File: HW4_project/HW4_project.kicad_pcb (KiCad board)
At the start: 2 copper layers, 50 x 50 mm, 26 parts, among them J1 CP2102, J2 BATT, J3 L, J4 R, J5 SCO, SW1 MCLR, SW2 SW_SPDT, SW3 USER, U1 AP7381-33V, U2 PIC32

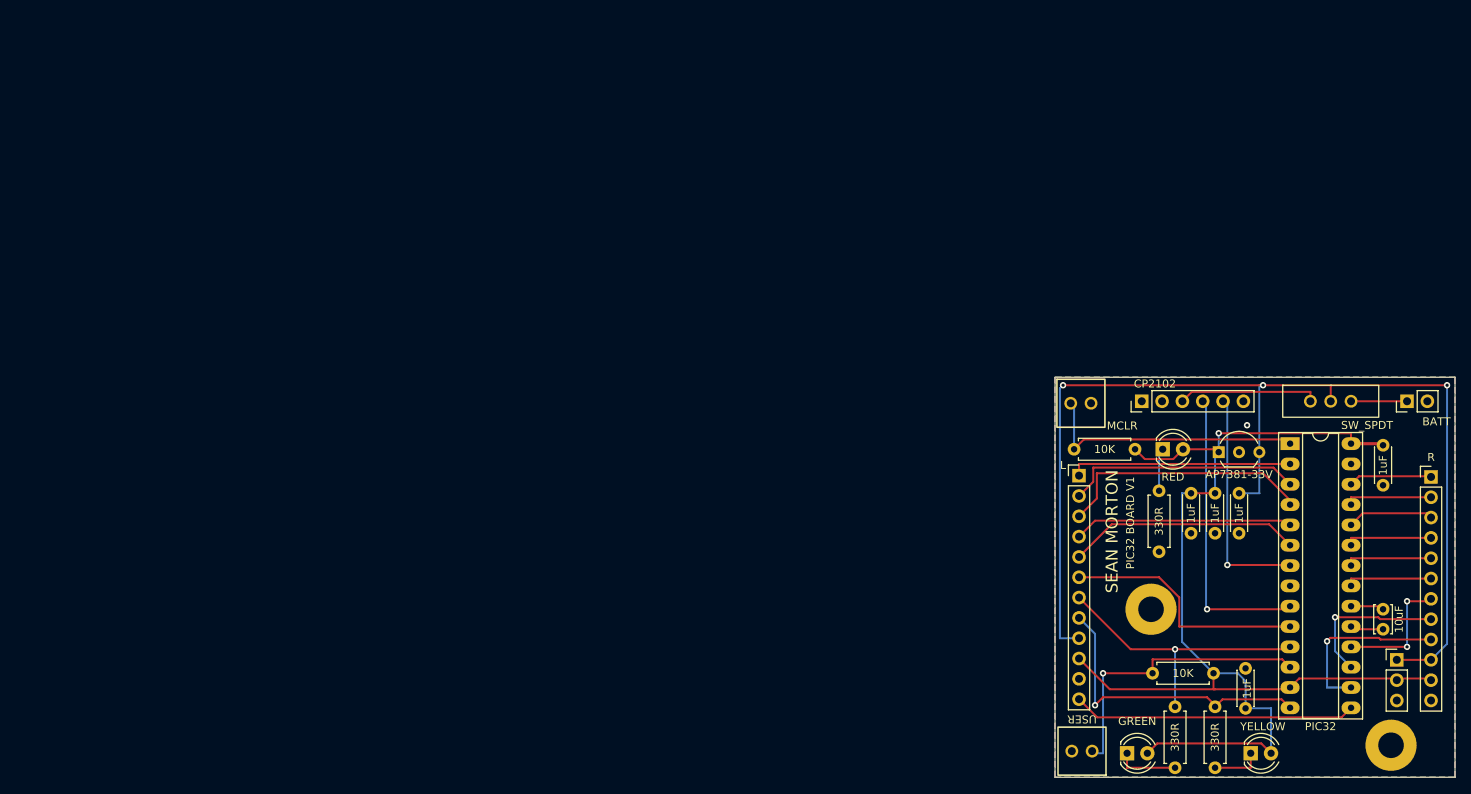
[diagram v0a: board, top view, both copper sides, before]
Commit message: HW4: silkscreen revisions
- added labels for all the broken-out pins
- fixed spacing on the button components
- added NURC logo
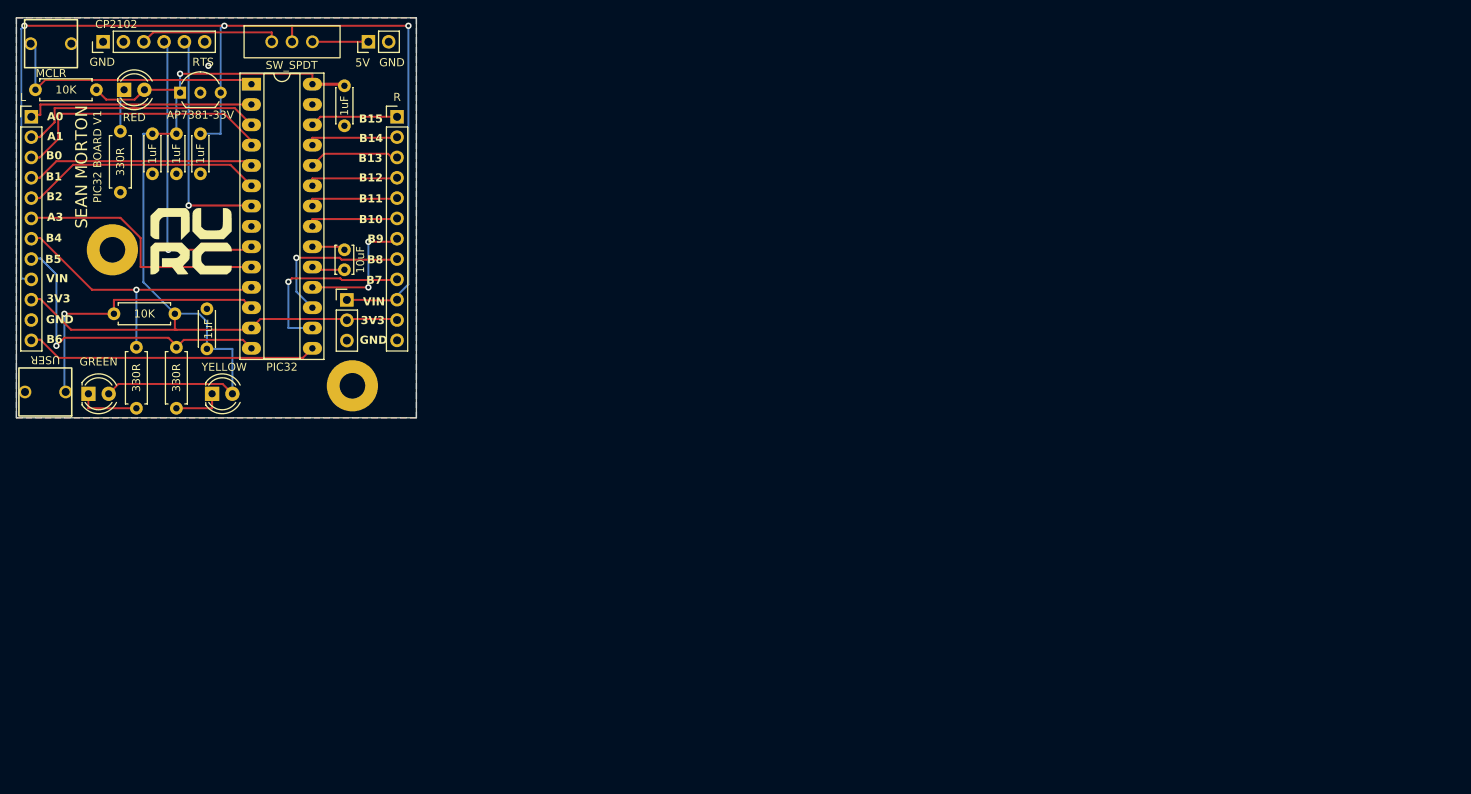
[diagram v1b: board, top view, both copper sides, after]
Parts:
- added G***: LOGO, HW4_footprints:logo_footprint_v3, F.Cu at (22.0, 28.0)
- moved J5 138.7 mm to (41.5, 35.3)
- moved J3 138.4 mm to (2.03, 12.4)
- moved C1 137.4 mm to (41.2, 8.57)
- moved C2 137.4 mm to (41.2, 29.1)
- moved D1 137.4 mm to (24.6, 47.1)
- moved D3 137.4 mm to (13.6, 9.07)
- moved H2 137.4 mm to (42.2, 46.1)
- moved J1 137.4 mm to (11.0, 3.07)
- moved J2 137.4 mm to (44.2, 3.07)
- moved SW2 137.4 mm to (34.6, 3.07)
- moved U1 137.4 mm to (20.6, 9.43)
- moved C3 137.4 mm to (20.2, 14.6)
- moved C4 137.4 mm to (17.2, 19.6)
- moved C5 137.4 mm to (24.0, 41.5)
- moved C7 137.4 mm to (23.2, 14.6)
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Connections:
- H2 pad 1: (no net) -> GND
- H3 pad 1: (no net) -> GND
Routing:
- net /RA1: track 29.8 -> 31.9 mm
- net /RA4_USER: track 37.3 -> 35.6 mm
- net /VDD5V0: track 139.2 -> 140.4 mm
- net /RB5_YLED: track 38.0 -> 39.1 mm
- net /RB4_GLED: track 36.5 -> 37.7 mm
- net /RB2: track 29.2 -> 30.3 mm
- net /RB0: track 32.4 -> 33.6 mm
- net /RA3: track 31.1 -> 32.2 mm
- net /RB1: track 27.4 -> 28.6 mm
- net /RB6: track 35.4 -> 36.6 mm
- net /VDD3V3: track 151.1 -> 152.3 mm
- net /RA0: track 27.8 -> 28.9 mm
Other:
- board text added: "3V3"
- board text added: "5V"
- board text added: "A0"
- board text added: "A1"
- board text added: "A3"
- board text added: "B0"
- board text added: "B1"
- board text added: "B10"
- board text added: "B11"
- board text added: "B12"
- board text added: "B13"
- board text added: "B14"
- board text added: "B15"
- board text added: "B2"
- board text added: "B4"
- board text added: "B5"
- board text added: "B6"
- board text added: "B7"
- board text added: "B8"
- board text added: "B9"
- board text added: "GND"
- board text added: "RTS"
- board text added: "VIN"

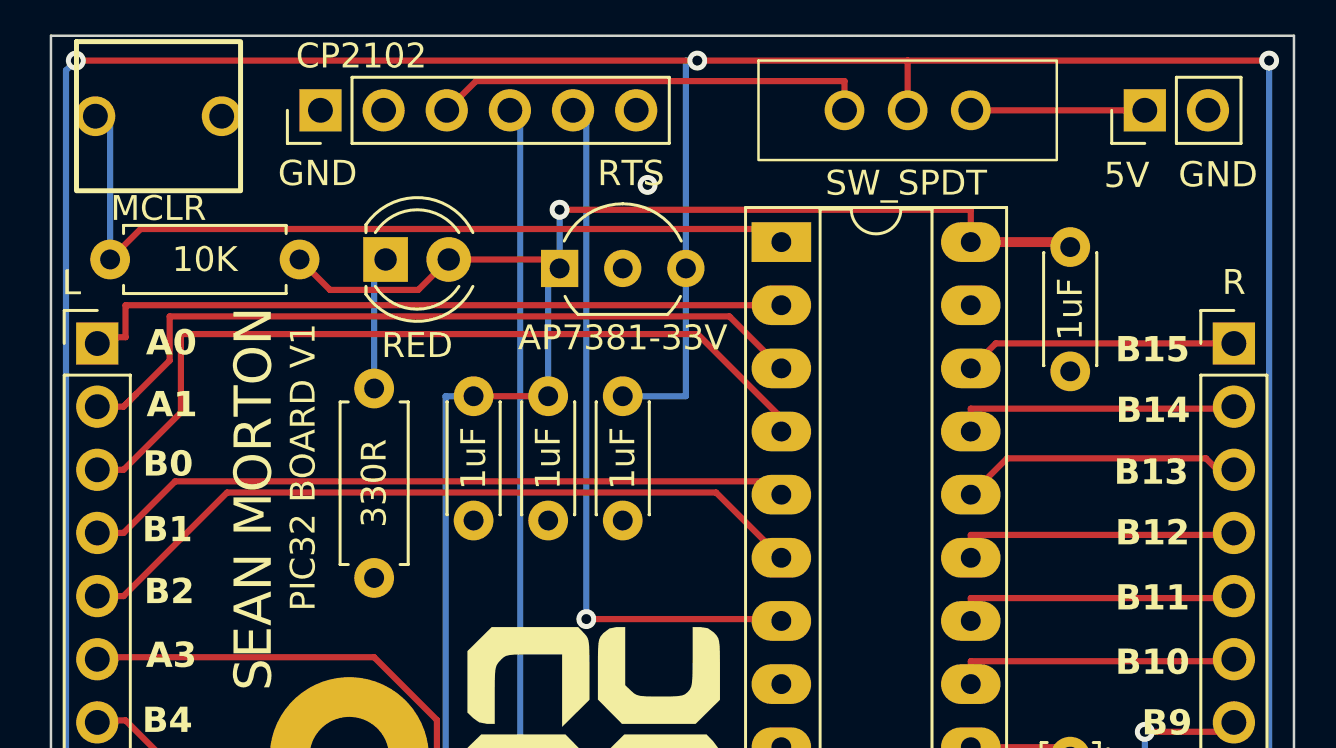
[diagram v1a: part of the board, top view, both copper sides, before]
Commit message: HW4 submission
- revised label for battery input voltage
- revised routing of 2 traces
- generated STEP file for robot modeling
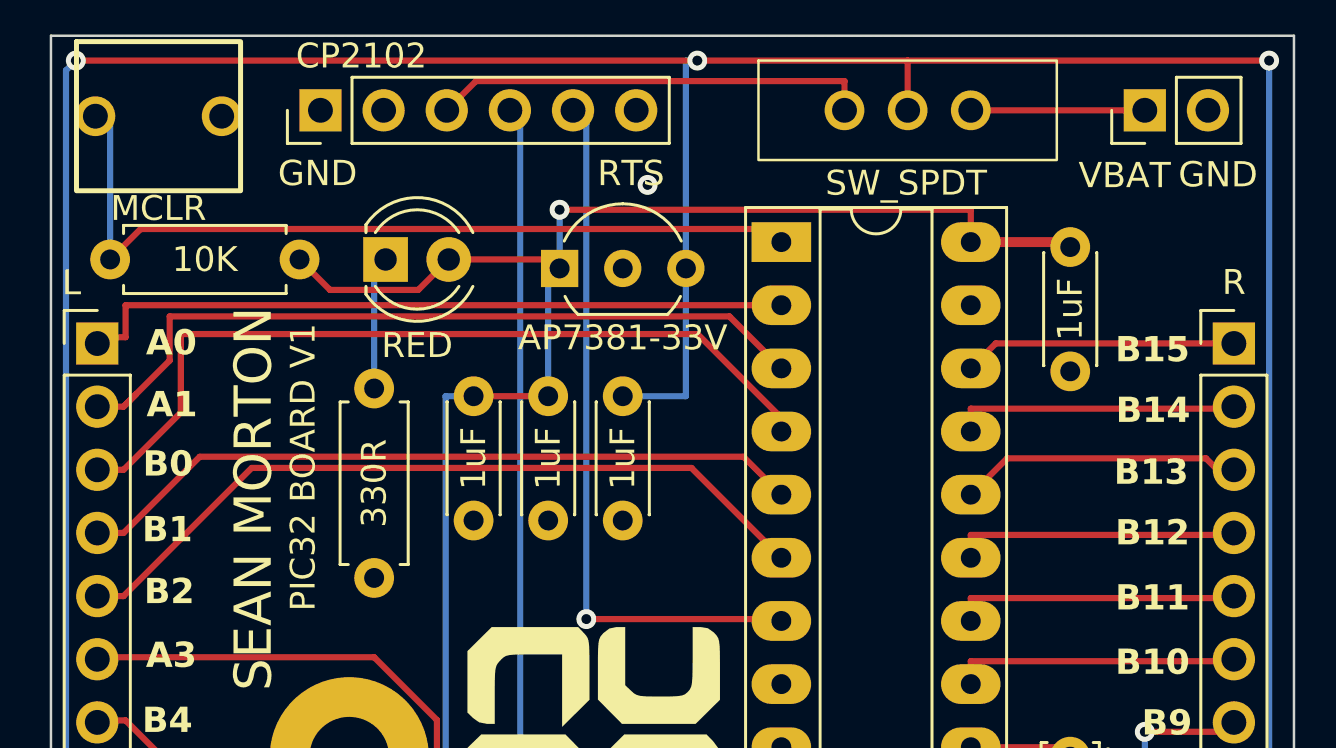
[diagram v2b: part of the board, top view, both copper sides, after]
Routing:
- net /RB2: track 30.3 -> 31.2 mm
- net /RB1: track 28.6 -> 29.4 mm
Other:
- board text added: "VBAT"
- board text removed: "5V"
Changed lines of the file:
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@@
     (effects (font (size 1.016 1.016) (thickness 0.254) bold) (justify left bottom))
   )
-  (gr_text "5V" (at 42.5196 6.2738) (layer "F.SilkS")
+  (gr_text "VBAT" (at 41.500084 6.28044) (layer "F.SilkS")
     (effects (font (size 1.016 1.016) (thickness 0.1524)) (justify left bottom))
   )
@@
   (segment (start 29.549 15.9854) (end 29.549 15.43639) (width 0.25) (layer "F.Cu") (net 15))
   (segment (start 3.0884 17.526) (end 2.032 17.526) (width 0.25) (layer "F.Cu") (net 15))
-  (segment (start 29.014 17.9904) (end 5.164 17.9904) (width 0.25) (layer "F.Cu") (net 16))
-  (segment (start 29.549 18.5254) (end 29.014 17.9904) (width 0.25) (layer "F.Cu") (net 16))
+  (segment (start 28.0236 17) (end 6.1544 17) (width 0.25) (layer "F.Cu") (net 16))
   (segment (start 3.0884 20.066) (end 2.032 20.066) (width 0.25) (layer "F.Cu") (net 16))
-  (segment (start 5.164 17.9904) (end 3.0884 20.066) (width 0.25) (layer "F.Cu") (net 16))
-  (segment (start 26.924 18.4404) (end 7.254 18.4404) (width 0.25) (layer "F.Cu") (net 17))
-  (segment (start 29.549 21.0654) (end 26.924 18.4404) (width 0.25) (layer "F.Cu") (net 17))
+  (segment (start 29.549 18.5254) (end 28.0236 17) (width 0.25) (layer "F.Cu") (net 16))
+  (segment (start 6.1544 17) (end 3.0884 20.066) (width 0.25) (layer "F.Cu") (net 16))
+  (segment (start 29.549 21.0654) (end 25.9336 17.45) (width 0.25) (layer "F.Cu") (net 17))
+  (segment (start 8.2444 17.45) (end 3.0884 22.606) (width 0.25) (layer "F.Cu") (net 17))
   (segment (start 3.0884 22.606) (end 2.032 22.606) (width 0.25) (layer "F.Cu") (net 17))
-  (segment (start 7.254 18.4404) (end 3.0884 22.606) (width 0.25) (layer "F.Cu") (net 17))
+  (segment (start 25.9336 17.45) (end 8.2444 17.45) (width 0.25) (layer "F.Cu") (net 17))
   (segment (start 21.704 23.5304) (end 29.549 23.5304) (width 0.25) (layer "F.Cu") (net 18))
   (segment (start 29.549 23.5304) (end 29.549 23.6054) (width 0.25) (layer "F.Cu") (net 18))
